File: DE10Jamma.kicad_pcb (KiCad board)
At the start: 2 copper layers, 114.6 x 83.4 mm, 106 parts, among them J1 Arduino 3-7, J10 5V TO DE10, J11 0.1" kick, J2 Arduino 8-SCL, J3 FAN 12V, J4 FAN 5V, J5 FAN 3V3, J6 Arduino Reset, J7 GPIO1, J8 Jamma_con, J9 CPS1 KICK, U1 TDA7496

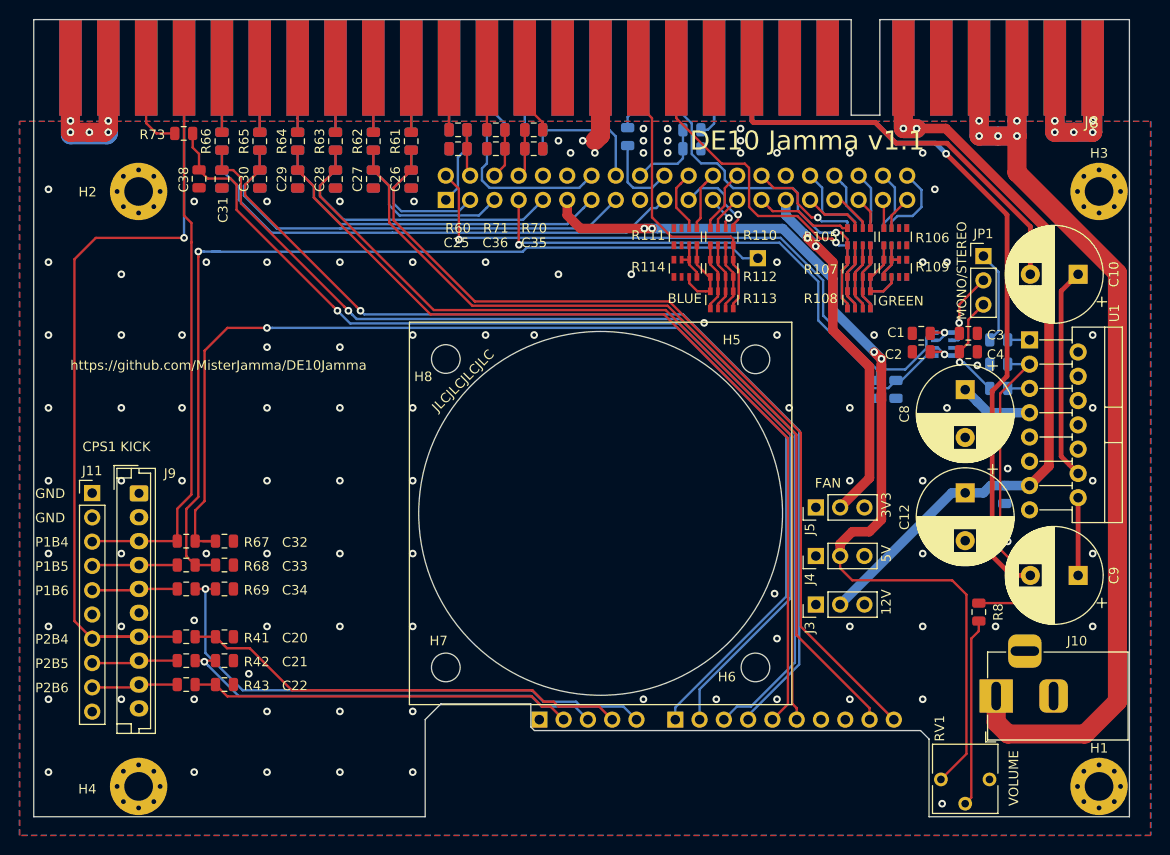
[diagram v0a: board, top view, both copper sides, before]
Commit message: single side assembly, swap out amplifier to a more common part, use common 0402 discrete resistors.
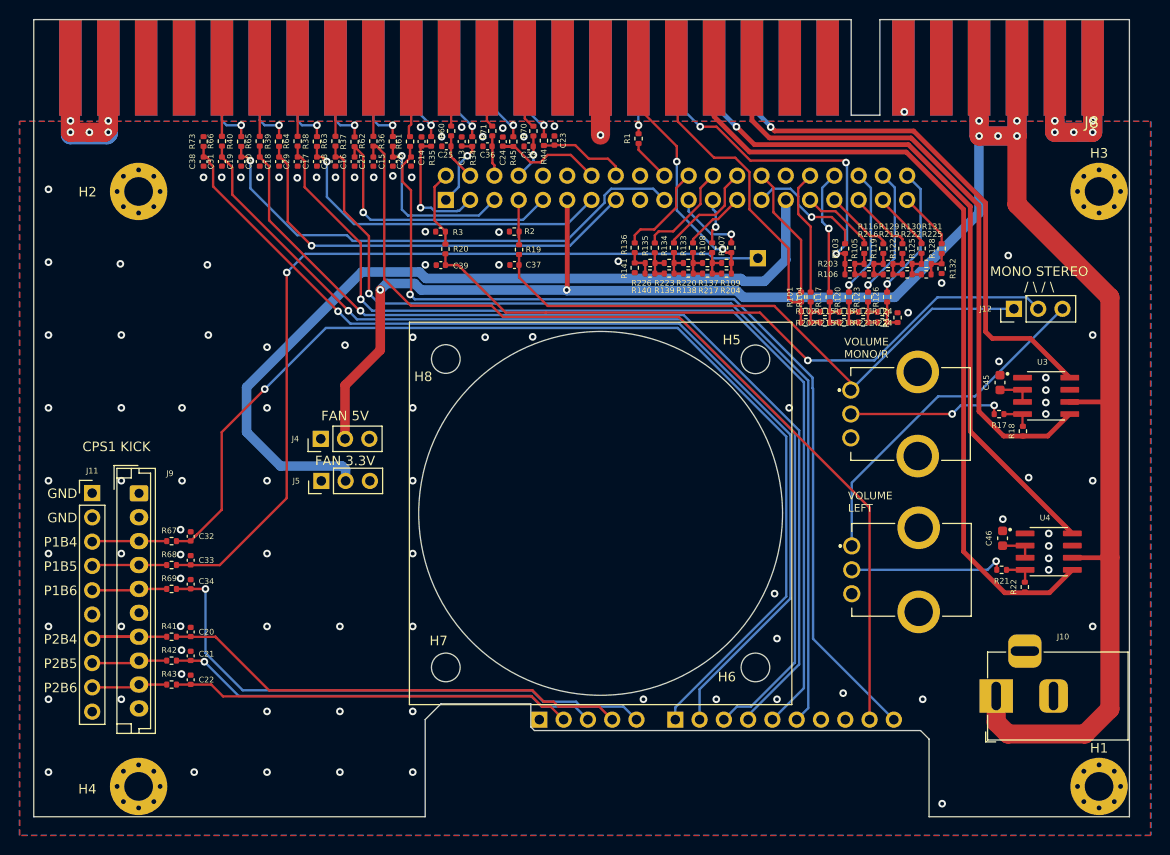
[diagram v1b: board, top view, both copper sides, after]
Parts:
- removed C1, C2, C3, C4: 10nF, Capacitor_SMD:C_0805_2012Metric
- removed C10, C12, C9: 1000uF, Capacitor_THT:CP_Radial_D10.0mm_P5.00mm
- removed C11, C7: 100nF, Capacitor_SMD:C_0805_2012Metric
- removed C5, C6: 470nF, Capacitor_SMD:C_0805_2012Metric
- removed C8: 470uF, Capacitor_THT:CP_Radial_D10.0mm_P5.00mm
- removed J3: FAN 12V, Connector_PinHeader_2.54mm:PinHeader_1x03_P2.54mm_Vertical
- removed JP1: Mono/Stereo, Connector_PinHeader_2.54mm:PinHeader_1x03_P2.54mm_Vertical
- removed R100, R110, R111, R112, R113, R114: 475R, Resistor_SMD:R_Array_Convex_4x0603
- removed R4: 560R, Resistor_SMD:R_Array_Convex_4x0603
- removed R72: 1k, Capacitor_SMD:C_0805_2012Metric
- removed R8: 300k, Capacitor_SMD:C_0805_2012Metric
- removed RV1: 50k, Potentiometer_THT:Potentiometer_Vishay_T73YP_Vertical
- removed U1: TDA7496, Package_TO_SOT_THT:TO-220-15_P2.54x2.54mm_StaggerOdd_Lead4.58mm_Vertical
- added C39: 20nF, Capacitor_SMD:C_0402_1005Metric, F.Cu at (130.2, 61.7)
- added C45: 1uF, Capacitor_SMD:C_0603_1608Metric, F.Cu at (188.6, 74.0)
- added C46: 1uF, Capacitor_SMD:C_0603_1608Metric, F.Cu at (188.9, 90.2)
- added G***: LOGO, LOGO, F.Cu at (106.3, 66.2)
- added J12: FAN 5V, Connector_PinHeader_2.54mm:PinHeader_1x03_P2.54mm_Vertical, F.Cu at (190.1, 66.2)
- added R115: 475R, Resistor_SMD:R_0402_1005Metric, F.Cu at (170.3, 67.7)
- added R116: 475R, Resistor_SMD:R_0402_1005Metric, F.Cu at (174.9, 61.5)
- added R117: 475R, Resistor_SMD:R_0402_1005Metric, F.Cu at (170.8, 65.0)
- added R118: 475R, Resistor_SMD:R_0402_1005Metric, F.Cu at (172.3, 67.7)
- added R119: 475R, Resistor_SMD:R_0402_1005Metric, F.Cu at (176.4, 60.0)
- added R120: 475R, Resistor_SMD:R_0402_1005Metric, F.Cu at (172.8, 65.0)
- added R121: 475R, Resistor_SMD:R_0402_1005Metric, F.Cu at (174.3, 67.7)
- added R122: 475R, Resistor_SMD:R_0402_1005Metric, F.Cu at (178.4, 60.0)
- added R123: 475R, Resistor_SMD:R_0402_1005Metric, F.Cu at (174.8, 65.0)
- added R124: 475R, Resistor_SMD:R_0402_1005Metric, F.Cu at (176.3, 67.7)
- added R125: 475R, Resistor_SMD:R_0402_1005Metric, F.Cu at (180.4, 59.9)
- added R126: 475R, Resistor_SMD:R_0402_1005Metric, F.Cu at (176.8, 65.0)
- added R127: 475R, Resistor_SMD:R_0402_1005Metric, F.Cu at (177.9, 67.2)
- added R128: 475R, Resistor_SMD:R_0402_1005Metric, F.Cu at (182.5, 60.0)
- added R129: 475R, Resistor_SMD:R_0402_1005Metric, F.Cu at (176.9, 61.5)
- added R130: 475R, Resistor_SMD:R_0402_1005Metric, F.Cu at (178.9, 61.5)
- added R131: 475R, Resistor_SMD:R_0402_1005Metric, F.Cu at (180.9, 61.5)
- added R132: 475R, Resistor_SMD:R_0402_1005Metric, F.Cu at (182.5, 62.0)
- added R133: 475R, Resistor_SMD:R_0402_1005Metric, F.Cu at (156.5, 59.9)
- added R134: 475R, Resistor_SMD:R_0402_1005Metric, F.Cu at (154.5, 59.9)
- added R135: 475R, Resistor_SMD:R_0402_1005Metric, F.Cu at (152.5, 59.9)
- added R136: 475R, Resistor_SMD:R_0402_1005Metric, F.Cu at (150.4, 59.9)
- added R137: 475R, Resistor_SMD:R_0402_1005Metric, F.Cu at (158.0, 61.5)
- added R138: 475R, Resistor_SMD:R_0402_1005Metric, F.Cu at (156.1, 62.6)
- added R139: 475R, Resistor_SMD:R_0402_1005Metric, F.Cu at (154.0, 62.6)
- added R140: 475R, Resistor_SMD:R_0402_1005Metric, F.Cu at (152.0, 62.6)
- added R141: 475R, Resistor_SMD:R_0402_1005Metric, F.Cu at (150.4, 62.0)
- added R17: 20k, Resistor_SMD:R_0402_1005Metric, F.Cu at (188.5, 77.3)
- added R18: 20k, Resistor_SMD:R_0402_1005Metric, F.Cu at (191.0, 79.0)
- added R19: 475R, Resistor_SMD:R_0402_1005Metric, F.Cu at (138.3, 60.1)
- added R20: 475R, Resistor_SMD:R_0402_1005Metric, F.Cu at (130.6, 60.0)
- added R202: 475R, Resistor_SMD:R_0402_1005Metric, F.Cu at (168.3, 66.6)
- added R203: 475R, Resistor_SMD:R_0402_1005Metric, F.Cu at (172.9, 61.5)
- added R204: 475R, Resistor_SMD:R_0402_1005Metric, F.Cu at (160.0, 62.6)
- added R21: 20k, Resistor_SMD:R_0402_1005Metric, F.Cu at (188.8, 93.5)
- added R215: 475R, Resistor_SMD:R_0402_1005Metric, F.Cu at (170.3, 66.6)
- added R216: 475R, Resistor_SMD:R_0402_1005Metric, F.Cu at (174.9, 62.6)
- added R217: 475R, Resistor_SMD:R_0402_1005Metric, F.Cu at (158.0, 62.6)
- added R218: 475R, Resistor_SMD:R_0402_1005Metric, F.Cu at (172.3, 66.6)
- added R219: 475R, Resistor_SMD:R_0402_1005Metric, F.Cu at (176.9, 62.6)
- added R22: 20k, Resistor_SMD:R_0402_1005Metric, F.Cu at (191.2, 95.3)
- added R220: 475R, Resistor_SMD:R_0402_1005Metric, F.Cu at (156.0, 61.5)
- added R221: 475R, Resistor_SMD:R_0402_1005Metric, F.Cu at (174.3, 66.6)
- added R222: 475R, Resistor_SMD:R_0402_1005Metric, F.Cu at (178.9, 62.6)
- added R223: 475R, Resistor_SMD:R_0402_1005Metric, F.Cu at (154.0, 61.5)
- added R224: 475R, Resistor_SMD:R_0402_1005Metric, F.Cu at (176.3, 66.6)
- added R225: 475R, Resistor_SMD:R_0402_1005Metric, F.Cu at (180.9, 62.6)
- added R226: 475R, Resistor_SMD:R_0402_1005Metric, F.Cu at (152.1, 61.5)
- added U3: LM4871MX_NOPB, LM4871MX_NOPB:SOIC127P599X175-8N, F.Cu at (193.5, 75.4)
- added U4: LM4871MX_NOPB, LM4871MX_NOPB:SOIC127P599X175-8N, F.Cu at (193.7, 91.7)
- added VR2: 50k, PTV09A-4020U-A503:PTV09A4020FB103, F.Cu at (178.6, 77.2)
- added VR3: 50k, PTV09A-4020U-A503:PTV09A4020FB103, F.Cu at (178.7, 93.5)
- C13, C14, C15, C16, C17, C18, C19, C23, C24: footprint Capacitor_SMD:C_0805_2012Metric -> Capacitor_SMD:C_0402_1005Metric; moved to F.Cu
- C20, C21, C22, C25, C26, C27, C28, C29, C30, C31, C32, C33, C34, C35, C36, C38: footprint Capacitor_SMD:C_0805_2012Metric -> Capacitor_SMD:C_0402_1005Metric
- C37: value 10nF -> 20nF; footprint Capacitor_SMD:C_0805_2012Metric -> Capacitor_SMD:C_0402_1005Metric; moved to F.Cu
- R1, R2, R3, R34, R35, R36, R37, R38, R39, R40, R44, R45: footprint Capacitor_SMD:C_0805_2012Metric -> Resistor_SMD:R_0402_1005Metric; moved to F.Cu
- R101, R102, R103, R104: footprint Resistor_SMD:R_Array_Convex_4x0603 -> Resistor_SMD:R_0402_1005Metric; moved to F.Cu
- R105, R106, R107, R108, R109: footprint Resistor_SMD:R_Array_Convex_4x0603 -> Resistor_SMD:R_0402_1005Metric
- R41, R42, R43, R60, R61, R62, R63, R64, R65, R66, R67, R68, R69, R70, R71, R73: footprint Capacitor_SMD:C_0805_2012Metric -> Resistor_SMD:R_0402_1005Metric
- moved J4 53.2 mm to (117.6, 79.8)
- moved J5 51.8 mm to (117.7, 84.2)
- moved R3 50.4 mm to (130.1, 58.2), turned to 0 degrees
- moved R2 41.4 mm to (137.8, 58.2), turned to 0 degrees
- moved C37 22.2 mm to (137.9, 61.7), turned to 0 degrees
- moved R109 17.7 mm to (160.0, 61.5), turned to 180 degrees
- moved R108 16.3 mm to (158.5, 59.9)
- moved R107 13.5 mm to (160.5, 59.9)
- moved R101 11.7 mm to (167.8, 65.0), turned to 90 degrees
- moved R104 9.35 mm to (168.8, 65.0), turned to 90 degrees
- moved R102 7.93 mm to (168.3, 67.7), turned to 0 degrees
- moved R106 6.17 mm to (172.9, 62.6), turned to 0 degrees
- moved R103 5.56 mm to (172.4, 60.0), turned to 90 degrees
- moved C14 4.08 mm to (128.1, 48.8), turned to -90 degrees
- moved C20 3.57 mm to (104.0, 100.0), turned to -90 degrees
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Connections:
- C37 pad 2: /TEST -> Net-(J12-Pin_1)
- J1 pad 1: (no net) -> unconnected-(J1-Pin_1-Pad1)
- J10 pad 1: +5VL -> +5V
- J11 pad 10: (no net) -> unconnected-(J11-Pin_10-Pad10)
- J11 pad 6: (no net) -> unconnected-(J11-Pin_6-Pad6)
- J2 pad 8: (no net) -> unconnected-(J2-Pin_8-Pad8)
- J4 pad 3: (no net) -> unconnected-(J4-Pin_3-Pad3)
- J5 pad 3: (no net) -> unconnected-(J5-Pin_3-Pad3)
- J7 pad 17: (no net) -> unconnected-(J7-Pin_17-Pad17)
- J8 pad 10: /JAMMA_SPEAKER_R -> /JAMMA_SPEAKER+
- J8 pad 11: (no net) -> /JAMMA_SPEAKER_L+
- J8 pad 15: (no net) -> unconnected-(J8-COIN_3-Pad15)
- J8 pad 25: /JAMMA_P1_BUTTON4 -> unconnected-(J8-P1_BUTTON_4-Pad25)
- J8 pad 26: /JAMMA_SELECT_UP -> unconnected-(J8-SELECT_UP-Pad26)
- J8 pad 3: +5VL -> +5V
- J8 pad 4: +5VL -> +5V
- J8 pad 5: (no net) -> unconnected-(J8--5V-Pad5)
- J8 pad 8: (no net) -> unconnected-(J8-COIN_COUNTER_1-Pad8)
- J8 pad 9: (no net) -> unconnected-(J8-COIN_LOCKOUT_1-Pad9)
- J8 pad C: +5VL -> +5V
- J8 pad D: +5VL -> +5V
- J8 pad E: (no net) -> unconnected-(J8--5V-PadE)
- J8 pad J: (no net) -> unconnected-(J8-COIN_COUNTER_2-PadJ)
- J8 pad K: (no net) -> unconnected-(J8-COIN_LOCKOUT_2-PadK)
- J8 pad L: /JAMMA_SPEAKER_L -> /JAMMA_SPEAKER-
- J8 pad M: /JAMMA_TEST -> /JAMMA_SPEAKER_L-
- J8 pad R: (no net) -> unconnected-(J8-SERVICE-PadR)
- J8 pad S: (no net) -> unconnected-(J8-COIN_4-PadS)
- J8 pad c: /JAMMA_P2_BUTTON4 -> unconnected-(J8-P2_BUTTON_4-Padc)
- J8 pad d: (no net) -> unconnected-(J8-SLECT_DOWN-Padd)
- J9 pad 10: (no net) -> unconnected-(J9-Pin_10-Pad10)
- J9 pad 6: (no net) -> unconnected-(J9-Pin_6-Pad6)
- R101 pad 1: /VIDEO_R3 -> /JAMMA_VIDEO_R
- R101 pad 2: /VIDEO_R2 -> /VIDEO_R7
- R102 pad 2: Net-(R100-Pad7) -> Net-(R102-Pad2)
- R103 pad 1: Net-(R100-Pad7) -> /JAMMA_VIDEO_G
- R103 pad 2: Net-(R100-Pad6) -> /VIDEO_G7
- R104 pad 1: Net-(R101-Pad8) -> Net-(R102-Pad2)
- R104 pad 2: Net-(R101-Pad7) -> /VIDEO_R6
- R105 pad 1: /JAMMA_VIDEO_G -> Net-(R105-Pad1)
- R105 pad 2: Net-(R105-Pad2) -> /VIDEO_G6
- R106 pad 1: Net-(R106-Pad1) -> /JAMMA_VIDEO_G
- R106 pad 2: Net-(R106-Pad2) -> Net-(R105-Pad1)
- R107 pad 1: Net-(R105-Pad2) -> /JAMMA_VIDEO_B
- R107 pad 2: Net-(R105-Pad3) -> /VIDEO_B7
- R108 pad 1: /JAMMA_VIDEO_G -> Net-(R108-Pad1)
- R108 pad 2: Net-(R105-Pad2) -> /VIDEO_B6
- R109 pad 1: Net-(R106-Pad2) -> /JAMMA_VIDEO_B
- R109 pad 2: Net-(R106-Pad1) -> Net-(R108-Pad1)
- R2 pad 2: /AUDIO_L -> /AUDIO_R
- R3 pad 2: /AUDIO_R -> /AUDIO_L
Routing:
- net +5V: track 105.7 -> 226.2 mm, vias 4 -> 7
- net +5VL: track 117.3 -> 0.00 mm, vias 5 -> 0
- net +12V: track 86.1 -> 0.00 mm, vias 2 -> 1
- net /JAMMA_SPEAKER_L+: track 0.00 -> 85.2 mm
- net /JAMMA_SPEAKER_L: track 77.5 -> 0.00 mm, vias 1 -> 0
- net /JAMMA_P2_BUTTON4: track 84.8 -> 11.9 mm, vias 1 -> 0
- net Net-(J12-Pin_2): track 0.00 -> 70.5 mm, vias 0 -> 1
- net /JAMMA_SPEAKER_L-: track 0.00 -> 69.8 mm, vias 0 -> 1
- net /JAMMA_SPEAKER+: track 0.00 -> 66.0 mm
- net Net-(J12-Pin_1): track 0.00 -> 63.0 mm
- net /AUDIO_L: track 68.6 -> 8.08 mm, vias 1 -> 0
- net /AUDIO_R: track 59.3 -> 5.30 mm, vias 1 -> 0
- net /JAMMA_SPEAKER-: track 0.00 -> 52.9 mm, vias 0 -> 1
- net /JAMMA_P1_BUTTON4: track 59.4 -> 7.88 mm
- net +3V3: track 38.3 -> 86.9 mm, vias 2 -> 0
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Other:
- net class Default removed
- net class Power removed
- rule pad_to_mask_clearance: 0.051 -> 0
- board text added: "DE10 JAMMA V2.0 (C)2025"
- board text added: "FAN 3.3V"
- board text added: "FAN 5V"
- board text added: "MONO STEREO / \ / \"
- board text added: "VOLUME LEFT"
- board text added: "VOLUME MONO/R"
- board text added: "github.com/MisterJamma/DE10Jamma"
- board text removed: "12V"
- board text removed: "3V3"
- board text removed: "5V"
- board text removed: "BLUE"
- board text removed: "DE10 Jamma v1.1"
- board text removed: "FAN"
- board text removed: "GREEN"
- board text removed: "JLCJLCJLCJLC"
- board text removed: "MONO/STEREO"
- board text removed: "VOLUME"
- board text removed: "https://github.com/MisterJamma/DE10Jamma"
